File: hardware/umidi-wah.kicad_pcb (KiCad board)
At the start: 2 copper layers, 129 x 107 mm, 88 parts, among them J1 Power, J2 Pots Main, J3 Pots Front, J4 Switch, J5 Input, J6 Output, J7 Conn_02x05_Odd_Even, J8 Conn_02x05_Odd_Even, K1 G6K-2P-Y-DC5, Q1 KSC1815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

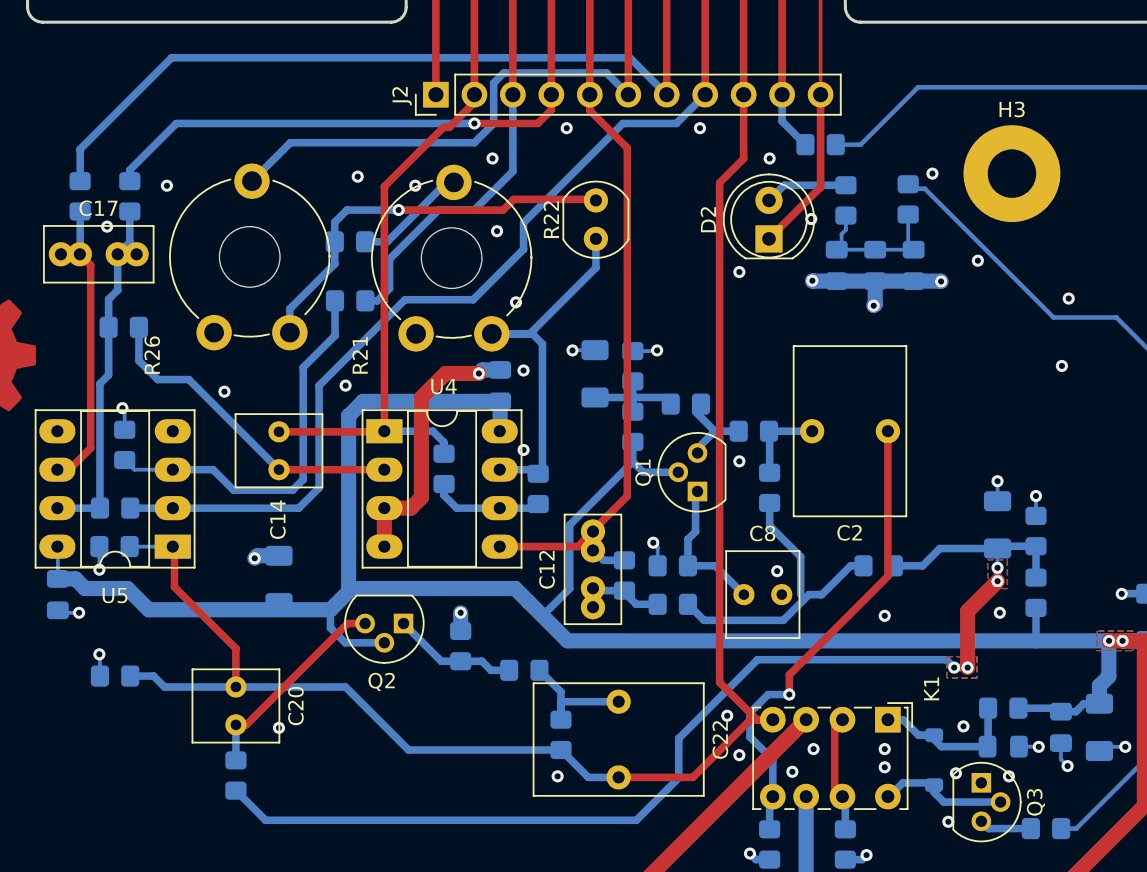
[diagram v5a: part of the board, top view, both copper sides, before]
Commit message: Optimize audio signal path
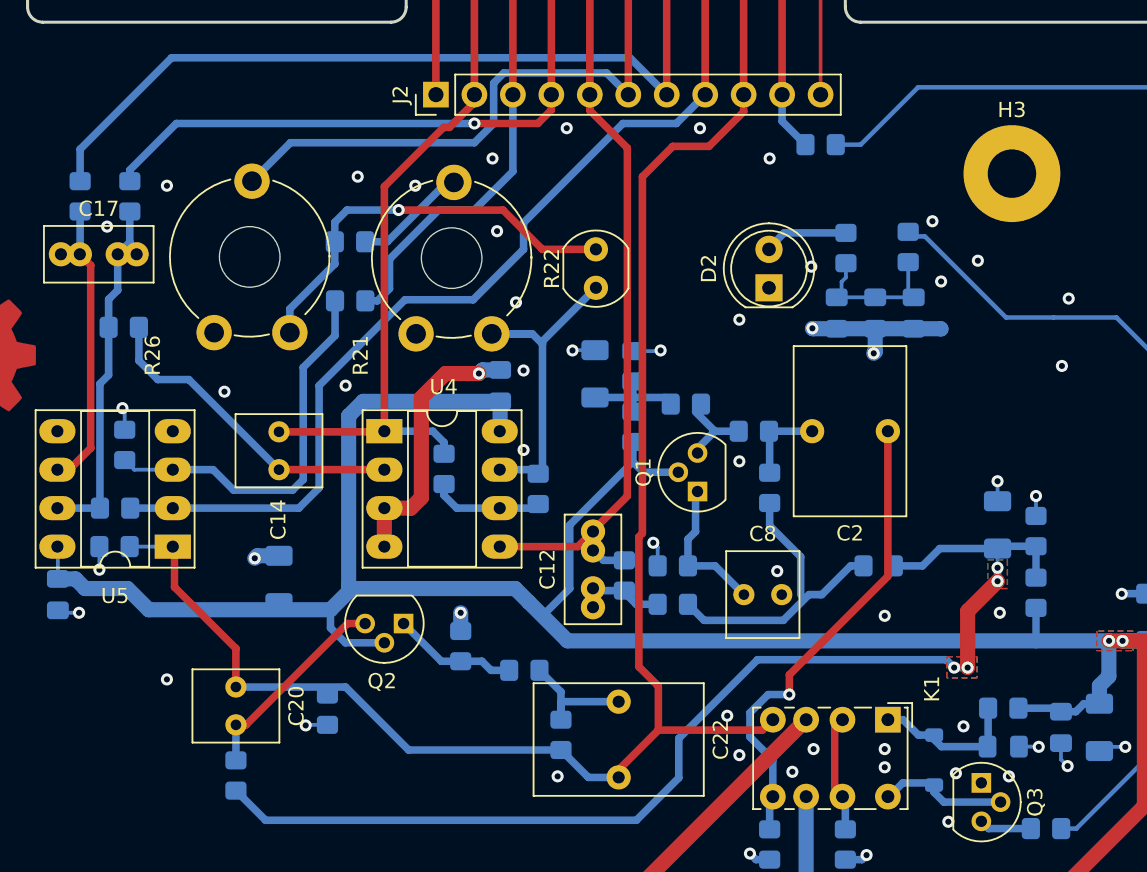
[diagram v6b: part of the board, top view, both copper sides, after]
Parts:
- moved R37 14.2 mm to (93.8, 98.4), turned to 90 degrees
- moved D2 3.23 mm to (123.0, 70.5)
- moved R22 3.23 mm to (111.5, 70.5)
- moved C13 3.14 mm to (127.4, 72.2)
- moved C15 3.14 mm to (130.0, 72.2)
- moved C16 3.14 mm to (132.5, 72.2)
- moved R12 3.14 mm to (132.2, 67.8)
- moved R18 3.14 mm to (128.0, 67.9)
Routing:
- net GND: track 164.3 -> 153.3 mm
- net /wah_out: track 151.4 -> 147.2 mm
- net Net-(R15-Pad2): track 25.6 -> 22.7 mm
- net /led_pwm: track 71.7 -> 70.4 mm
- net Net-(R22-Pad2): track 26.4 -> 27.2 mm

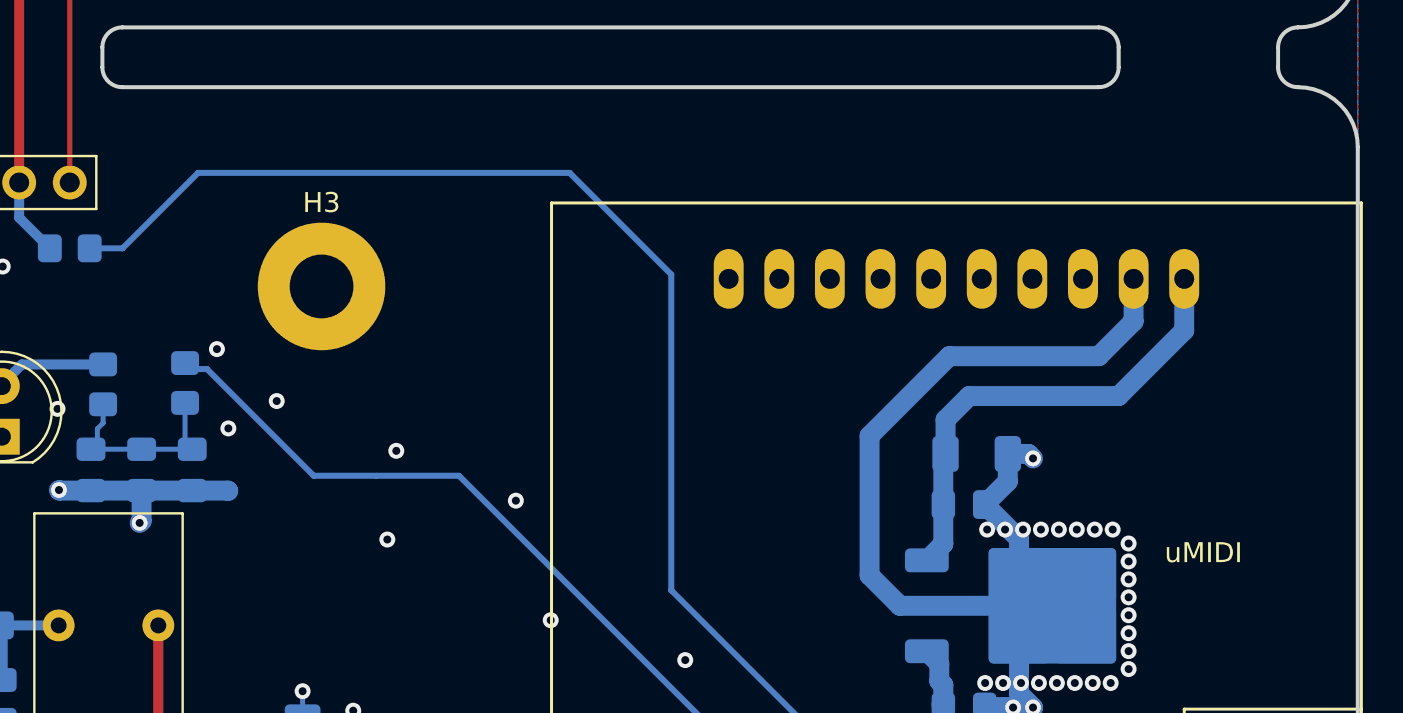
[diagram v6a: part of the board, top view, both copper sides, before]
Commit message: Add solder holes for midi signals
Now, it is possible to make the entire umidi-pcba pluggable.
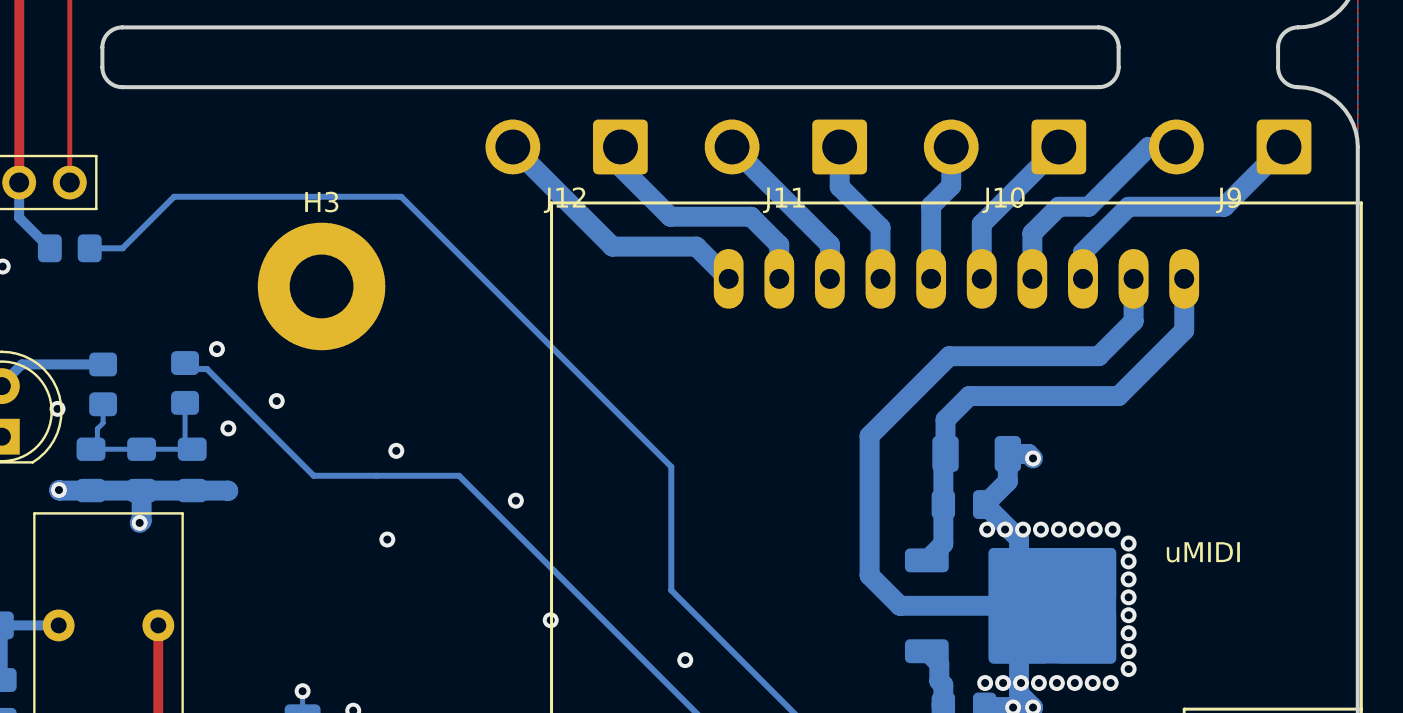
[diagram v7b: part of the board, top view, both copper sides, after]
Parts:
- added J10: Midi_thru, Connector_Wire:SolderWire-1sqmm_1x02_P5.4mm_D1.4mm_OD2.7mm, F.Cu at (176.0, 56.0)
- added J11: Midi_t/o, Connector_Wire:SolderWire-1sqmm_1x02_P5.4mm_D1.4mm_OD2.7mm, F.Cu at (165.0, 56.0)
- added J12: Midi_out, Connector_Wire:SolderWire-1sqmm_1x02_P5.4mm_D1.4mm_OD2.7mm, F.Cu at (154.0, 56.0)
- added J9: Midi_in, Connector_Wire:SolderWire-1sqmm_1x02_P5.4mm_D1.4mm_OD2.7mm, F.Cu at (187.3, 56.0)
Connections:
- BRD1 pad 10: unconnected-(BRD1A-MIDI_out--Pad10) -> Net-(BRD1A-MIDI_out-)
- BRD1 pad 3: unconnected-(BRD1A-MIDI_in+-Pad3) -> Net-(BRD1A-MIDI_in+)
- BRD1 pad 4: unconnected-(BRD1A-MIDI_in--Pad4) -> Net-(BRD1A-MIDI_in-)
- BRD1 pad 5: unconnected-(BRD1A-MIDI_thru+-Pad5) -> Net-(BRD1A-MIDI_thru+)
- BRD1 pad 6: unconnected-(BRD1A-MIDI_thru--Pad6) -> Net-(BRD1A-MIDI_thru-)
- BRD1 pad 7: unconnected-(BRD1A-MIDI_T/O+-Pad7) -> Net-(BRD1A-MIDI_T/O+)
- BRD1 pad 8: unconnected-(BRD1A-MIDI_T/O--Pad8) -> Net-(BRD1A-MIDI_T/O-)
- BRD1 pad 9: unconnected-(BRD1A-MIDI_out+-Pad9) -> Net-(BRD1A-MIDI_out+)
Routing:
- net Net-(BRD1A-MIDI_in+): track 0.00 -> 13.6 mm
- net Net-(BRD1A-MIDI_out-): track 0.00 -> 13.6 mm
- net Net-(BRD1A-MIDI_out+): track 0.00 -> 12.3 mm
- net Net-(BRD1A-MIDI_in-): track 0.00 -> 11.3 mm
- net Net-(BRD1A-MIDI_T/O-): track 0.00 -> 8.65 mm
- net Net-(BRD1A-MIDI_thru+): track 0.00 -> 8.22 mm
- net Net-(BRD1A-MIDI_T/O+): track 0.00 -> 7.47 mm
- net Net-(BRD1A-MIDI_thru-): track 0.00 -> 7.04 mm
- net /Filter/status_led: track 87.5 -> 80.9 mm
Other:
- board text added: "midi in"
- board text added: "midi out"
- board text added: "midi thru"
- board text added: "thru/out"
